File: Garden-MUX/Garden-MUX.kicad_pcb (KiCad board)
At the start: 2 copper layers, 46 x 46 mm, 53 parts, among them J1 USB_C_Receptacle_USB2.0_16P, J2 SDCARD_MODULE, P1 S2B-PH-SM4-TB, Q1 AO3401A, U2 MCP73832-2-OT, U3 AP2112K-3.3, U4 AP2112K-3.3, U5 ESP32-C6-MINI-1

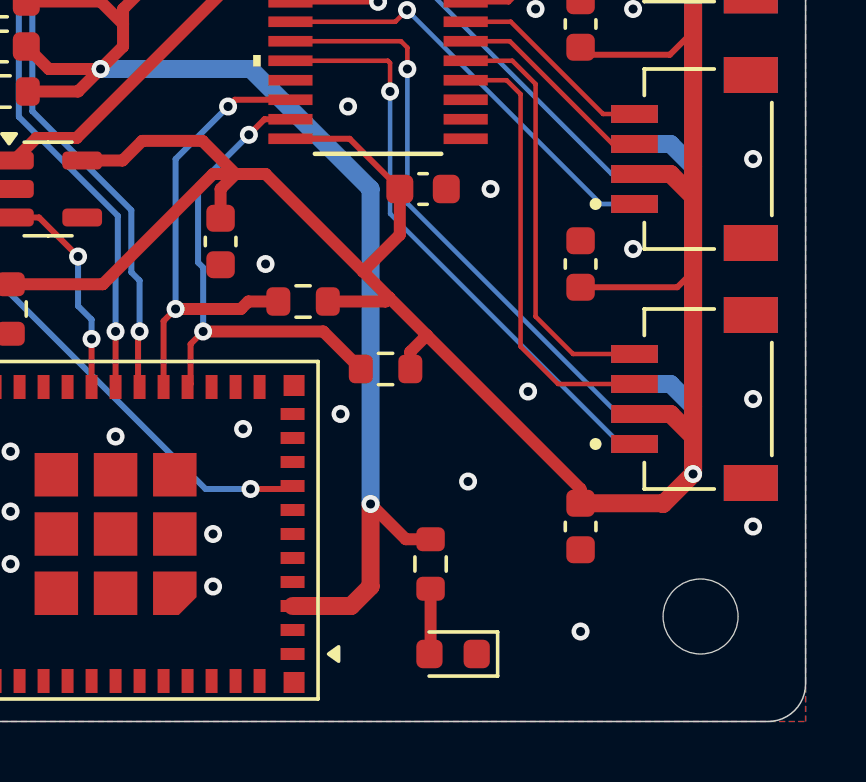
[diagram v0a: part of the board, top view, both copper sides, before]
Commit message: Transfer capacitors from 4 layer board
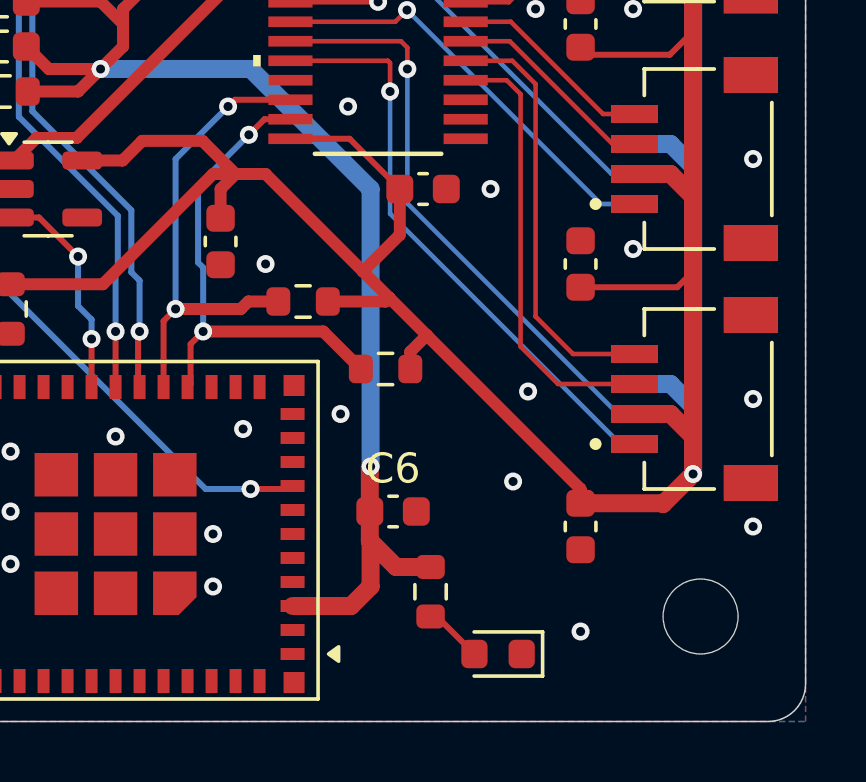
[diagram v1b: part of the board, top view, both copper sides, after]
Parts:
- added C6: 1, Capacitor_SMD:C_0603_1608Metric, F.Cu at (163.5, 101.2)
- moved D1 1.50 mm to (167.0, 106.0)
- moved R3 0.92 mm to (164.8, 103.9)
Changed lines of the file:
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@@
 		)
 	)
+	(footprint "Capacitor_SMD:C_0603_1608Metric"
+		(layer "F.Cu")
+		(at 163.5 101.25)
+		(descr "Capacitor SMD 0603 (1608 Metric), square (rectangular) end terminal, IPC-7351 nominal, (Body size source: IPC-SM-782 page 76, https://www.pcb-3d.com/wordpress/wp-content/uploads/ipc-sm-782a_amendment_1_and_2.pdf), generated with kicad-footprint-generator")
+		(tags "capacitor")
+		(property "Reference" "C6"
+			(at 0 -1.43 0)
+			(layer "F.SilkS")
+			(effects
+				(font
+					(size 1 1)
+					(thickness 0.15)
+				)
+			)
+		)
+		(property "Value" "1"
+			(at 0 1.43 0)
+			(layer "F.Fab")
+			(effects
+				(font
+					(size 1 1)
+					(thickness 0.15)
+				)
+			)
+		)
+		(property "Datasheet" ""
+			(at 0 0 0)
+			(layer "F.Fab")
+			(hide yes)
+			(effects
+				(font
+					(size 1.27 1.27)
+					(thickness 0.15)
+				)
+			)
+		)
+		(property "Description" "Unpolarized capacitor"
+			(at 0 0 0)
+			(layer "F.Fab")
+			(hide yes)
+			(effects
+				(font
+					(size 1.27 1.27)
+					(thickness 0.15)
+				)
+			)
+		)
+		(property ki_fp_filters "C_*")
+		(sheetname "/")
+		(sheetfile "Garden-MUX.kicad_sch")
+		(attr smd)
+		(fp_line
+			(start -0.14058 -0.51)
+			(end 0.14058 -0.51)
+			(stroke
+				(width 0.12)
+				(type solid)
+			)
+			(layer "F.SilkS")
+		)
+		(fp_line
+			(start -0.14058 0.51)
+			(end 0.14058 0.51)
+			(stroke
+				(width 0.12)
+				(type solid)
+			)
+			(layer "F.SilkS")
+		)
+		(fp_line
+			(start -1.48 -0.73)
+			(end 1.48 -0.73)
+			(stroke
+				(width 0.05)
+				(type solid)
+			)
+			(layer "F.CrtYd")
+		)
+		(fp_line
+			(start -1.48 0.73)
+			(end -1.48 -0.73)
+			(stroke
+				(width 0.05)
+				(type solid)
+			)
+			(layer "F.CrtYd")
+		)
+		(fp_line
+			(start 1.48 -0.73)
+			(end 1.48 0.73)
+			(stroke
+				(width 0.05)
+				(type solid)
+			)
+			(layer "F.CrtYd")
+		)
+		(fp_line
+			(start 1.48 0.73)
+			(end -1.48 0.73)
+			(stroke
+				(width 0.05)
+				(type solid)
+			)
+			(layer "F.CrtYd")
+		)
+		(fp_line
+			(start -0.8 -0.4)
+			(end 0.8 -0.4)
+			(stroke
+				(width 0.1)
+				(type solid)
+			)
+			(layer "F.Fab")
+		)
+		(fp_line
+			(start -0.8 0.4)
+			(end -0.8 -0.4)
+			(stroke
+				(width 0.1)
+				(type solid)
+			)
+			(layer "F.Fab")
+		)
+		(fp_line
+			(start 0.8 -0.4)
+			(end 0.8 0.4)
+			(stroke
+				(width 0.1)
+				(type solid)
+			)
+			(layer "F.Fab")
+		)
+		(fp_line
+			(start 0.8 0.4)
+			(end -0.8 0.4)
+			(stroke
+				(width 0.1)
+				(type solid)
+			)
+			(layer "F.Fab")
+		)
+		(fp_text user "${REFERENCE}"
+			(at 0 0 0)
+			(layer "F.Fab")
+			(effects
+				(font
+					(size 0.4 0.4)
+					(thickness 0.06)
+				)
+			)
+		)
+		(pad "1" smd roundrect
+			(at -0.775 0)
+			(size 0.9 0.95)
+			(layers "F.Cu" "F.Mask" "F.Paste")
+			(roundrect_rratio 0.25)
+			(net 3 "+3.3V")
+			(pintype "passive")
+		)
+		(pad "2" smd roundrect
+			(at 0.775 0)
+			(size 0.9 0.95)
+			(layers "F.Cu" "F.Mask" "F.Paste")
+			(roundrect_rratio 0.25)
+			(net 1 "GND")
+			(pintype "passive")
+		)
+		(embedded_fonts no)
+		(model "${KICAD9_3DMODEL_DIR}/Capacitor_SMD.3dshapes/C_0603_1608Metric.step"
+			(offset
+				(xyz 0 0 0)
+			)
+			(scale
+				(xyz 1 1 1)
+			)
+			(rotate
+				(xyz 0 0 0)
+			)
+		)
+	)
 	(footprint "Pico_Footprints:STEMMAQWIIC_Footprint"
 		(layer "F.Cu")
@@
 	(footprint "Resistor_SMD:R_0603_1608Metric"
 		(layer "F.Cu")
-		(at 164.75 103 -90)
+		(at 164.75 103.925 -90)
 		(descr "Resistor SMD 0603 (1608 Metric), square (rectangular) end terminal, IPC-7351 nominal, (Body size source: IPC-SM-782 page 72, https://www.pcb-3d.com/wordpress/wp-content/uploads/ipc-sm-782a_amendment_1_and_2.pdf), generated with kicad-footprint-generator")
 		(tags "resistor")
@@
 	(footprint "LED_SMD:LED_0603_1608Metric"
 		(layer "F.Cu")
-		(at 165.5 106 180)
+		(at 167 106 180)
 		(descr "LED SMD 0603 (1608 Metric), square (rectangular) end terminal, IPC-7351 nominal, (Body size source: http://www.tortai-tech.com/upload/download/2011102023233369053.pdf), generated with kicad-footprint-generator")
 		(tags "LED")
@@
 	)
 	(via
-		(at 166 100.25)
+		(at 167.5 100.25)
 		(size 0.6)
 		(drill 0.3)
@@
 	)
 	(segment
+		(start 162.75 103.75)
+		(end 162.1 104.4)
+		(width 0.6)
+		(layer "F.Cu")
+		(net 3)
+	)
+	(segment
 		(start 154.5 85)
 		(end 154.5 85.75)
@@
 	)
 	(segment
+		(start 162.725 99.775)
+		(end 162.75 99.75)
+		(width 0.6)
+		(layer "F.Cu")
+		(net 3)
+	)
+	(segment
+		(start 162.725 102.225)
+		(end 162.725 101.25)
+		(width 0.6)
+		(layer "F.Cu")
+		(net 3)
+	)
+	(segment
+		(start 162.75 102.25)
+		(end 162.725 102.225)
+		(width 0.6)
+		(layer "F.Cu")
+		(net 3)
+	)
+	(segment
 		(start 155.45 83)
 		(end 155.45 83.55)
@@
 	)
 	(segment
+		(start 162.725 101.25)
+		(end 162.725 99.775)
+		(width 0.6)
+		(layer "F.Cu")
+		(net 3)
+	)
+	(segment
 		(start 154.5 84.5)
 		(end 154.5 85)
@@
 	)
 	(segment
-		(start 162.75 101)
-		(end 162.75 103.75)
+		(start 162.1 104.4)
+		(end 160.15 104.4)
 		(width 0.6)
 		(layer "F.Cu")
@@
 	)
 	(segment
-		(start 164.75 102.175)
-		(end 163.925 102.175)
-		(width 0.4)
-		(layer "F.Cu")
-		(net 3)
-	)
-	(segment
 		(start 152.025 86.5)
 		(end 151.275 85.75)
@@
 	)
 	(segment
-		(start 162.1 104.4)
-		(end 160.15 104.4)
+		(start 162.75 102.25)
+		(end 162.75 103.75)
 		(width 0.6)
 		(layer "F.Cu")
@@
 	)
 	(segment
-		(start 163.925 102.175)
-		(end 162.75 101)
-		(width 0.4)
-		(layer "F.Cu")
-		(net 3)
-	)
-	(segment
 		(start 153.75 84.25)
 		(end 154.5 85)
@@
 	)
 	(segment
-		(start 162.75 103.75)
-		(end 162.1 104.4)
-		(width 0.6)
+		(start 151.275 84.25)
+		(end 153.75 84.25)
+		(width 0.4)
 		(layer "F.Cu")
 		(net 3)
 	)
 	(segment
-		(start 151.275 84.25)
-		(end 153.75 84.25)
-		(width 0.4)
+		(start 163.6 103.1)
+		(end 164.75 103.1)
+		(width 0.6)
 		(layer "F.Cu")
 		(net 3)
@@
 		(net 3)
 	)
+	(segment
+		(start 162.75 102.25)
+		(end 163.6 103.1)
+		(width 0.6)
+		(layer "F.Cu")
+		(net 3)
+	)
 	(via
-		(at 162.75 101)
+		(at 162.75 99.75)
 		(size 0.6)
 		(drill 0.3)
@@
 	)
 	(segment
-		(start 158.75 86.5)
-		(end 153.75 86.5)
+		(start 162.75 90.5)
+		(end 158.75 86.5)
 		(width 0.6)
 		(layer "B.Cu")
@@
 	)
 	(segment
-		(start 162.75 101)
+		(start 162.75 99.75)
 		(end 162.75 90.5)
 		(width 0.6)
@@
 	)
 	(segment
-		(start 162.75 90.5)
-		(end 158.75 86.5)
+		(start 158.75 86.5)
+		(end 153.75 86.5)
 		(width 0.6)
 		(layer "B.Cu")
@@
 	)
 	(segment
-		(start 164.75 103.825)
-		(end 164.75 105.9625)
-		(width 0.4)
-		(layer "F.Cu")
-		(net 6)
-	)
-	(segment
-		(start 164.75 105.9625)
-		(end 164.7125 106)
-		(width 0.4)
+		(start 164.75 104.5375)
+		(end 166.2125 106)
+		(width 0.2)
 		(layer "F.Cu")
 		(net 6)

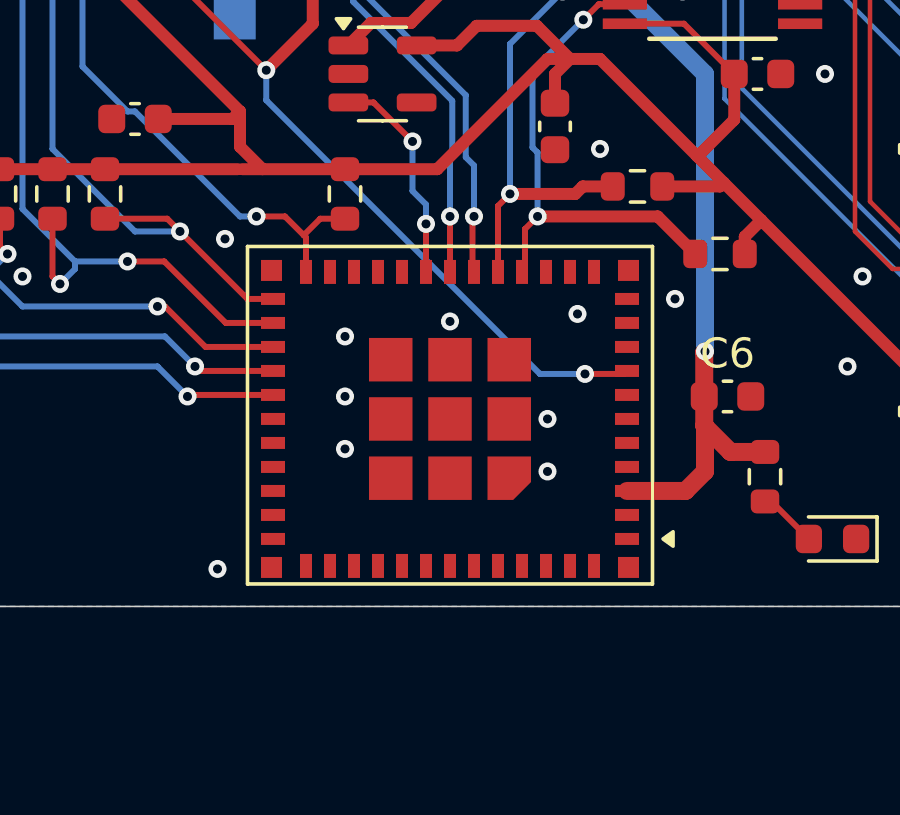
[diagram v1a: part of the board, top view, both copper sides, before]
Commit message: Update 3D models file locations to global
The 3D models file paths no longer need to modified to be seen
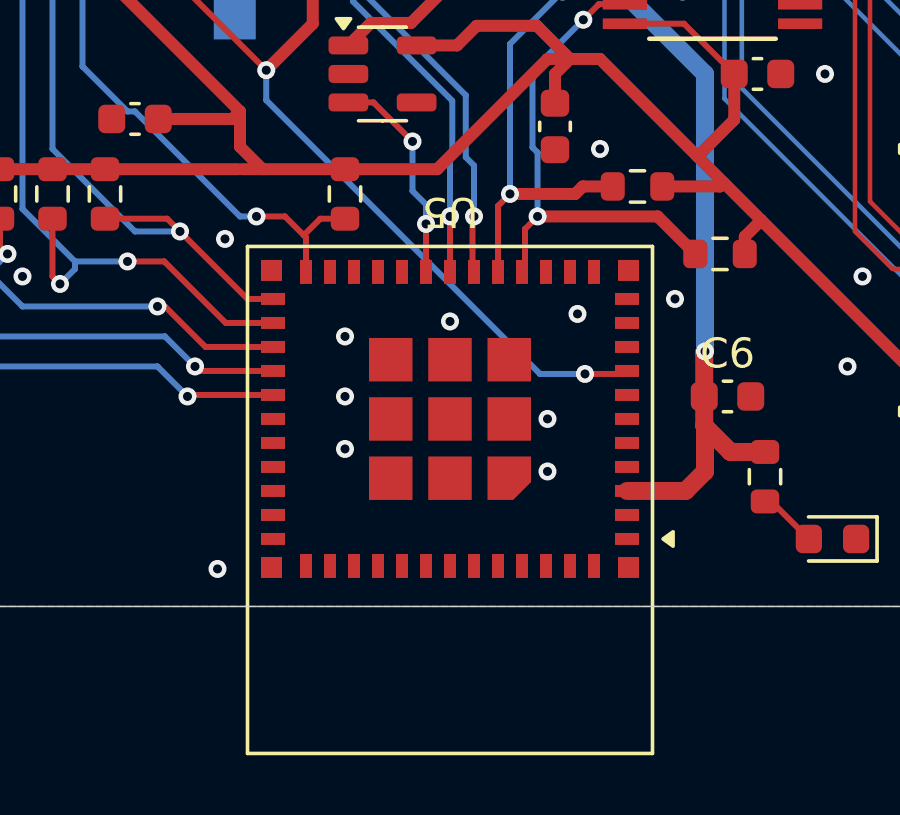
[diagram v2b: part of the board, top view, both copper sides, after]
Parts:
- U5: footprint RF_Module:ESP32-C6-MINI-1 -> Pico_Footprints:ESP32-C6-MINI-1
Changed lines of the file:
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@@
 			(psa4output no)
 			(plot_black_and_white yes)
+			(plotinvisibletext no)
 			(sketchpadsonfab no)
 			(plotpadnumbers no)
@@
 		)
 	)
-	(footprint "RF_Module:ESP32-C6-MINI-1"
+	(footprint "Pico_Footprints:ESP32-C6-MINI-1"
 		(layer "F.Cu")
 		(at 154.25 102 180)
@@
 			(at 0 6.9 180)
 			(unlocked yes)
-			(layer "F.Fab")
+			(layer "F.SilkS")
 			(effects
 				(font
@@
 		)
 		(property "Value" "ESP32-C6-MINI-1"
-			(at 2.25 6.9 180)
+			(at 0 6.9 180)
 			(unlocked yes)
 			(layer "F.Fab")
@@
 		)
 		(fp_line
-			(start 6.75 -5.5)
+			(start 6.75 -11.15)
 			(end 6.75 5.75)
 			(stroke
@@
 		(fp_line
 			(start -6.75 5.75)
-			(end -6.75 -5.5)
+			(end -6.75 -11.15)
 			(stroke
 				(width 0.12)
@@
 		)
 		(fp_line
-			(start -6.75 -5.5)
-			(end 6.75 -5.5)
+			(start -6.75 -11.15)
+			(end 6.75 -11.15)
 			(stroke
 				(width 0.12)
@@
 		)
 		(fp_text user "Antenna"
-			(at 0 -7.675 0)
+			(at 0 -7.675 180)
 			(layer "Cmts.User")
 			(effects
@@
 		)
 		(fp_text user "Keepout Area"
-			(at -0.01 -15.36 0)
+			(at -0.01 -15.36 180)
 			(layer "Cmts.User")
 			(effects
@@
 		)
 		(embedded_fonts no)
-		(model "/Users/sunewst/Documents/GitHub/Garden-microcontroller/REIMAGINED_3D_FILES_BLENDER/ESP32-C6-MINI-1-N4.step"
+		(model "${KICA}/ESP32-C6-MINI-1-N4.step"
 			(offset
 				(xyz 0 0 0)
